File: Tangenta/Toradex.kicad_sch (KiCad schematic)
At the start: 16 parts, among them J17 2309410-1, Q3 BSS138, T1 NTZD3154NT1G

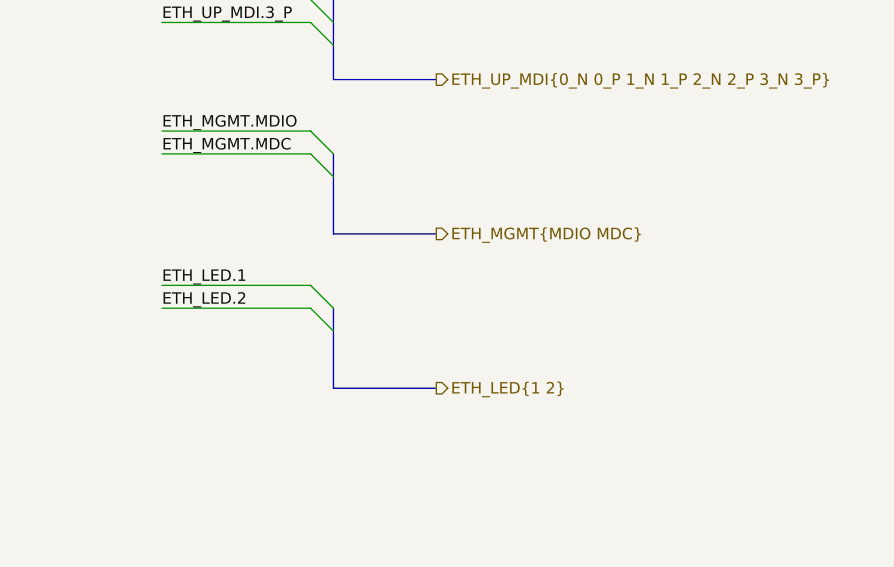
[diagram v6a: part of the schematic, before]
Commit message: Ethernet Switch schematic done, ports TBD...
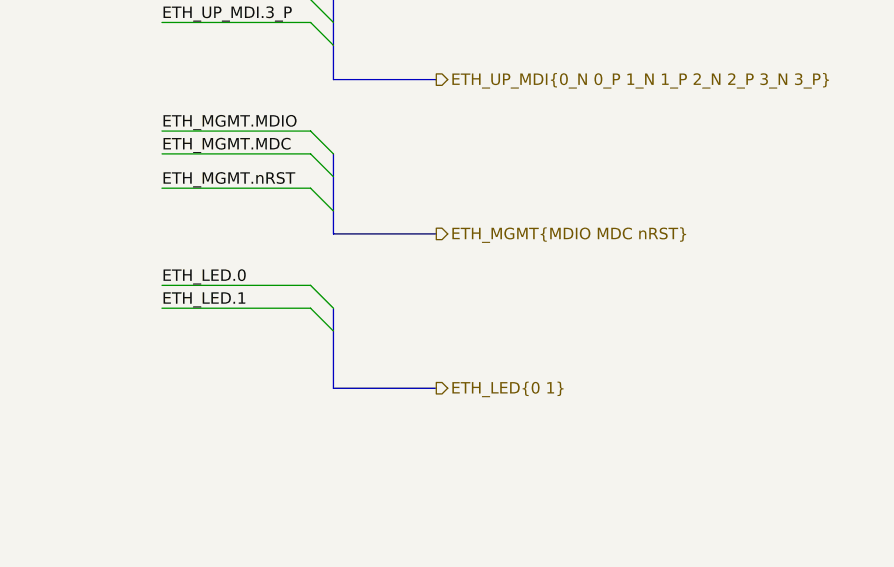
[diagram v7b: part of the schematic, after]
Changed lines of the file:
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@@
+    (stroke (width 0) (type default))
+  )
+  (bus_entry (at 341.63 228.6) (size -2.54 -2.54)
     (stroke (width 0) (type default))
   )
@@
     (stroke (width 0) (type default))
   )
-  (bus (pts (xy 341.63 224.79) (xy 341.63 231.14))
+  (bus (pts (xy 341.63 224.79) (xy 341.63 228.6))
     (stroke (width 0) (type default))
   )
@@
     (stroke (width 0) (type default))
   )
+  (bus (pts (xy 341.63 228.6) (xy 341.63 231.14))
+    (stroke (width 0) (type default))
+  )
   (wire (pts (xy 90.17 148.59) (xy 90.17 167.64))
     (stroke (width 0) (type default))
@@
     (stroke (width 0) (type default))
   )
+  (wire (pts (xy 322.58 226.06) (xy 339.09 226.06))
+    (stroke (width 0) (type default))
+  )
   (bus (pts (xy 359.41 40.64) (xy 359.41 43.18))
     (stroke (width 0) (type default))
@@
     (effects (font (size 1.27 1.27)) (justify left bottom))
   )
-  (label "ETH_LED.2" (at 322.58 239.395 0) (fields_autoplaced)
+  (label "ETH_LED.1" (at 322.58 239.395 0) (fields_autoplaced)
     (effects (font (size 1.27 1.27)) (justify left bottom))
   )
@@
     (effects (font (size 1.27 1.27)) (justify left bottom))
   )
+  (label "ETH_MGMT.nRST" (at 322.58 226.06 0) (fields_autoplaced)
+    (effects (font (size 1.27 1.27)) (justify left bottom))
+  )
   (label "I2C_2_DSI.SDA" (at 181.61 167.64 90) (fields_autoplaced)
     (effects (font (size 1.27 1.27)) (justify left bottom))
@@
     (effects (font (size 1.27 1.27)) (justify left bottom))
   )
-  (label "ETH_LED.1" (at 322.58 236.855 0) (fields_autoplaced)
+  (label "ETH_LED.0" (at 322.58 236.855 0) (fields_autoplaced)
     (effects (font (size 1.27 1.27)) (justify left bottom))
   )
@@
     (effects (font (size 1.27 1.27)) (justify left))
   )
-  (hierarchical_label "ETH_LED{1 2}" (shape output) (at 353.06 248.285 0) (fields_autoplaced)
+  (hierarchical_label "ETH_LED{0 1}" (shape output) (at 353.06 248.285 0) (fields_autoplaced)
     (effects (font (size 1.27 1.27)) (justify left))
   )
@@
     (effects (font (size 1.27 1.27)) (justify left))
   )
-  (hierarchical_label "ETH_MGMT{MDIO MDC}" (shape output) (at 353.06 231.14 0) (fields_autoplaced)
-    (effects (font (size 1.27 1.27)) (justify left))
-  )
+  (hierarchical_label "ETH_MGMT{MDIO MDC nRST}" (shape output) (at 353.06 231.14 0) (fields_autoplaced)
+    (effects (font (size 1.27 1.27)) (justify left))
+  )

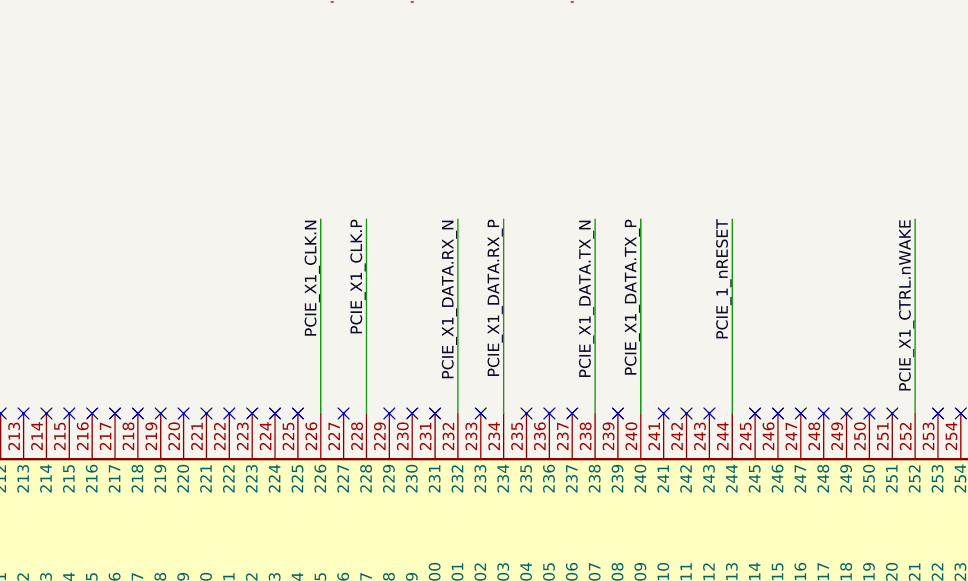
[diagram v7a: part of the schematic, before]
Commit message: Assigned Eth netclasses, MDIO and Toradex connections.
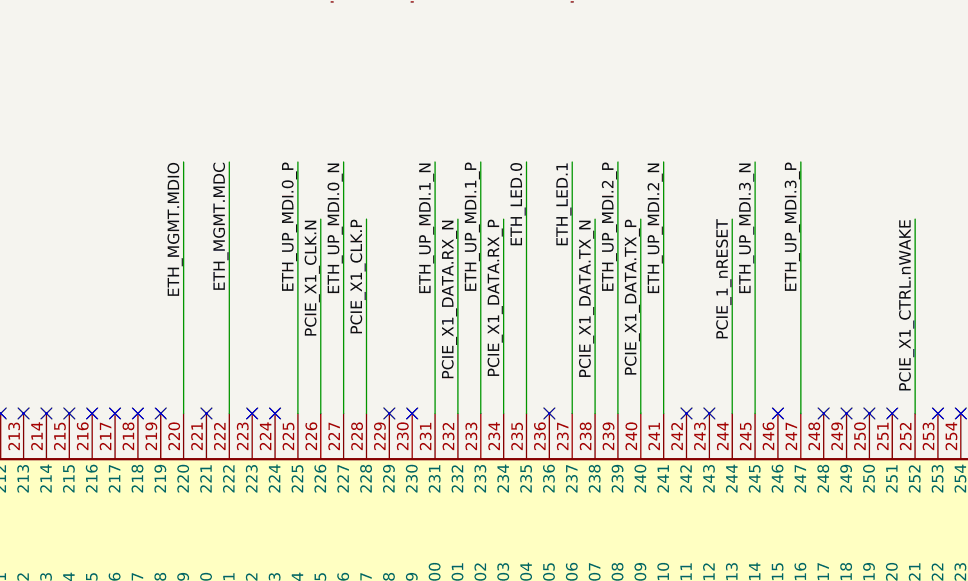
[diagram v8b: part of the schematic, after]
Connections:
- net ETH_LED.0: now also J17.235
- net ETH_LED.1: now also J17.237
- net ETH_MGMT.MDC: now also J17.222
- net ETH_MGMT.MDIO: now also J17.220
- net ETH_UP_MDI.0_N: now also J17.227
- net ETH_UP_MDI.0_P: now also J17.225
- net ETH_UP_MDI.1_N: now also J17.231
- net ETH_UP_MDI.1_P: now also J17.233
- net ETH_UP_MDI.2_N: now also J17.241
- net ETH_UP_MDI.2_P: now also J17.239
- net ETH_UP_MDI.3_N: now also J17.245
- net ETH_UP_MDI.3_P: now also J17.247
- no-connect marks 226 -> 214
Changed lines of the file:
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@@
   (no_connect (at 265.43 148.59))
   (no_connect (at 135.89 123.19))
-  (no_connect (at 341.63 123.19))
   (no_connect (at 349.25 148.59))
   (no_connect (at 138.43 123.19))
@@
   (no_connect (at 285.75 148.59))
   (no_connect (at 102.87 148.59))
-  (no_connect (at 326.39 123.19))
   (no_connect (at 334.01 148.59))
   (no_connect (at 217.17 123.19))
@@
   (no_connect (at 265.43 123.19))
   (no_connect (at 90.17 123.19))
-  (no_connect (at 273.05 123.19))
   (no_connect (at 242.57 148.59))
   (no_connect (at 196.85 123.19))
@@
   (no_connect (at 359.41 123.19))
   (no_connect (at 207.01 148.59))
-  (no_connect (at 311.15 123.19))
   (no_connect (at 69.85 123.19))
   (no_connect (at 328.93 148.59))
@@
   (no_connect (at 275.59 123.19))
   (no_connect (at 349.25 123.19))
-  (no_connect (at 300.99 123.19))
   (no_connect (at 234.95 148.59))
   (no_connect (at 372.11 148.59))
@@
   (no_connect (at 156.21 123.19))
   (no_connect (at 367.03 148.59))
-  (no_connect (at 321.31 123.19))
   (no_connect (at 115.57 123.19))
   (no_connect (at 323.85 148.59))
   (no_connect (at 74.93 123.19))
-  (no_connect (at 285.75 123.19))
   (no_connect (at 283.21 148.59))
   (no_connect (at 222.25 123.19))
@@
   (no_connect (at 97.79 123.19))
   (no_connect (at 107.95 148.59))
-  (no_connect (at 316.23 123.19))
   (no_connect (at 64.77 123.19))
   (no_connect (at 275.59 148.59))
@@
   (no_connect (at 351.79 148.59))
   (no_connect (at 222.25 148.59))
-  (no_connect (at 336.55 123.19))
   (no_connect (at 69.85 148.59))
   (no_connect (at 64.77 148.59))
@@
   (no_connect (at 364.49 123.19))
   (no_connect (at 161.29 123.19))
-  (no_connect (at 306.07 123.19))
   (no_connect (at 179.07 148.59))
   (no_connect (at 181.61 123.19))
@@
   (no_connect (at 229.87 123.19))
   (no_connect (at 133.35 148.59))
-  (no_connect (at 290.83 123.19))
   (no_connect (at 280.67 123.19))
   (no_connect (at 354.33 148.59))
@@
   (no_connect (at 240.03 148.59))
   (no_connect (at 346.71 148.59))
-  (no_connect (at 278.13 123.19))
   (no_connect (at 240.03 123.19))
   (no_connect (at 311.15 148.59))
@@
     (stroke (width 0) (type default))
   )
+  (wire (pts (xy 316.23 95.25) (xy 316.23 123.19))
+    (stroke (width 0) (type default))
+  )
   (bus (pts (xy 341.63 192.405) (xy 341.63 194.945))
     (stroke (width 0) (type default))
@@
     (stroke (width 0) (type default))
   )
+  (wire (pts (xy 336.55 95.25) (xy 336.55 123.19))
+    (stroke (width 0) (type default))
+  )
   (wire (pts (xy 153.67 148.59) (xy 153.67 167.64))
     (stroke (width 0) (type default))
@@
     (stroke (width 0) (type default))
   )
+  (wire (pts (xy 273.05 95.25) (xy 273.05 123.19))
+    (stroke (width 0) (type default))
+  )
   (wire (pts (xy 316.23 55.88) (xy 316.23 52.07))
     (stroke (width 0) (type default))
@@
     (stroke (width 0) (type default))
   )
+  (wire (pts (xy 278.13 95.25) (xy 278.13 123.19))
+    (stroke (width 0) (type default))
+  )
   (wire (pts (xy 120.65 36.83) (xy 104.14 36.83))
     (stroke (width 0) (type default))
@@
     (stroke (width 0) (type default))
   )
+  (wire (pts (xy 290.83 95.25) (xy 290.83 123.19))
+    (stroke (width 0) (type default))
+  )
   (bus (pts (xy 341.63 207.645) (xy 341.63 210.185))
     (stroke (width 0) (type default))
@@
     (stroke (width 0) (type default))
   )
+  (wire (pts (xy 341.63 95.25) (xy 341.63 123.19))
+    (stroke (width 0) (type default))
+  )
   (wire (pts (xy 76.2 236.22) (xy 76.2 240.03))
     (stroke (width 0) (type default))
@@
     (stroke (width 0) (type default))
   )
+  (wire (pts (xy 311.15 95.25) (xy 311.15 123.19))
+    (stroke (width 0) (type default))
+  )
   (wire (pts (xy 173.99 123.19) (xy 173.99 104.14))
     (stroke (width 0) (type default))
@@
     (stroke (width 0) (type default))
   )
+  (wire (pts (xy 285.75 95.25) (xy 285.75 123.19))
+    (stroke (width 0) (type default))
+  )
   (wire (pts (xy 298.45 73.66) (xy 298.45 74.93))
     (stroke (width 0) (type default))
@@
     (stroke (width 0) (type default))
   )
+  (wire (pts (xy 306.07 95.25) (xy 306.07 123.19))
+    (stroke (width 0) (type default))
+  )
+  (wire (pts (xy 326.39 95.25) (xy 326.39 123.19))
+    (stroke (width 0) (type default))
+  )
   (bus (pts (xy 40.64 30.48) (xy 40.64 33.02))
     (stroke (width 0) (type default))
@@
     (stroke (width 0) (type default))
   )
+  (wire (pts (xy 321.31 95.25) (xy 321.31 123.19))
+    (stroke (width 0) (type default))
+  )
   (wire (pts (xy 62.23 260.35) (xy 62.23 265.43))
     (stroke (width 0) (type default))
@@
     (stroke (width 0) (type default))
   )
+  (wire (pts (xy 300.99 95.25) (xy 300.99 123.19))
+    (stroke (width 0) (type default))
+  )
   (wire (pts (xy 76.2 210.82) (xy 59.69 210.82))
     (stroke (width 0) (type default))
@@
     (effects (font (size 1.27 1.27)) (justify left bottom))
   )
+  (label "ETH_MGMT.MDIO" (at 273.05 95.25 270) (fields_autoplaced)
+    (effects (font (size 1.27 1.27)) (justify right bottom))
+  )
   (label "3V3" (at 306.07 52.07 0) (fields_autoplaced)
     (effects (font (size 1.27 1.27)) (justify left bottom))
@@
     (effects (font (size 1.27 1.27)) (justify left bottom))
   )
+  (label "ETH_UP_MDI.1_P" (at 306.07 95.25 270) (fields_autoplaced)
+    (effects (font (size 1.27 1.27)) (justify right bottom))
+  )
   (label "USB_DR.VBUS" (at 20.32 22.86 0) (fields_autoplaced)
     (effects (font (size 1.27 1.27)) (justify left bottom))
@@
     (effects (font (size 1.27 1.27)) (justify left bottom))
   )
+  (label "ETH_MGMT.MDC" (at 278.13 95.25 270) (fields_autoplaced)
+    (effects (font (size 1.27 1.27)) (justify right bottom))
+  )
   (label "PCIE_X1_CLK.P" (at 341.63 17.78 0) (fields_autoplaced)
     (effects (font (size 1.27 1.27)) (justify left bottom))
@@
     (effects (font (size 1.27 1.27)) (justify right bottom))
   )
+  (label "ETH_UP_MDI.2_P" (at 321.31 95.25 270) (fields_autoplaced)
+    (effects (font (size 1.27 1.27)) (justify right bottom))
+  )
   (label "3V3" (at 24.13 198.12 0) (fields_autoplaced)
     (effects (font (size 1.27 1.27)) (justify left bottom))
@@
     (effects (font (size 1.27 1.27)) (justify left bottom))
   )
+  (label "ETH_UP_MDI.3_P" (at 341.63 95.25 270) (fields_autoplaced)
+    (effects (font (size 1.27 1.27)) (justify right bottom))
+  )
   (label "I2C_1.SCL" (at 24.13 210.82 0) (fields_autoplaced)
     (effects (font (size 1.27 1.27)) (justify left bottom))
@@
     (effects (font (size 1.27 1.27)) (justify left bottom))
   )
+  (label "ETH_LED.1" (at 316.23 95.25 270) (fields_autoplaced)
+    (effects (font (size 1.27 1.27)) (justify right bottom))
+  )
   (label "DSI.CLK_N" (at 135.89 167.64 90) (fields_autoplaced)
     (effects (font (size 1.27 1.27)) (justify left bottom))
@@
     (effects (font (size 1.27 1.27)) (justify left bottom))
   )
+  (label "ETH_LED.0" (at 311.15 95.25 270) (fields_autoplaced)
+    (effects (font (size 1.27 1.27)) (justify right bottom))
+  )
   (label "I2C_2_DSI.SCL" (at 21.59 93.98 0) (fields_autoplaced)
     (effects (font (size 1.27 1.27)) (justify left bottom))
@@
     (effects (font (size 1.27 1.27)) (justify left bottom))
   )
+  (label "ETH_UP_MDI.0_N" (at 290.83 95.25 270) (fields_autoplaced)
+    (effects (font (size 1.27 1.27)) (justify right bottom))
+  )
   (label "ETH_UP_MDI.3_N" (at 322.58 205.105 0) (fields_autoplaced)
     (effects (font (size 1.27 1.27)) (justify left bottom))
@@
     (effects (font (size 1.27 1.27)) (justify right bottom))
   )
+  (label "ETH_UP_MDI.3_N" (at 336.55 95.25 270) (fields_autoplaced)
+    (effects (font (size 1.27 1.27)) (justify right bottom))
+  )
   (label "PCIE_X1_CLK.N" (at 341.63 21.59 0) (fields_autoplaced)
     (effects (font (size 1.27 1.27)) (justify left bottom))
@@
     (effects (font (size 1.27 1.27)) (justify left bottom))
   )
+  (label "ETH_UP_MDI.2_N" (at 326.39 95.25 270) (fields_autoplaced)
+    (effects (font (size 1.27 1.27)) (justify right bottom))
+  )
   (label "DSI.INT" (at 104.14 57.15 0) (fields_autoplaced)
     (effects (font (size 1.27 1.27)) (justify left bottom))
@@
     (effects (font (size 1.27 1.27)) (justify right bottom))
   )
+  (label "ETH_UP_MDI.1_N" (at 300.99 95.25 270) (fields_autoplaced)
+    (effects (font (size 1.27 1.27)) (justify right bottom))
+  )
   (label "ETH_UP_MDI.0_P" (at 322.58 192.405 0) (fields_autoplaced)
     (effects (font (size 1.27 1.27)) (justify left bottom))
@@
     (effects (font (size 1.27 1.27)) (justify left bottom))
   )
+  (label "ETH_UP_MDI.0_P" (at 285.75 95.25 270) (fields_autoplaced)
+    (effects (font (size 1.27 1.27)) (justify right bottom))
+  )
   (label "PCIE_X1_DATA.RX_P" (at 339.09 35.56 0) (fields_autoplaced)
